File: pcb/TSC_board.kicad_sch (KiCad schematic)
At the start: 29 parts

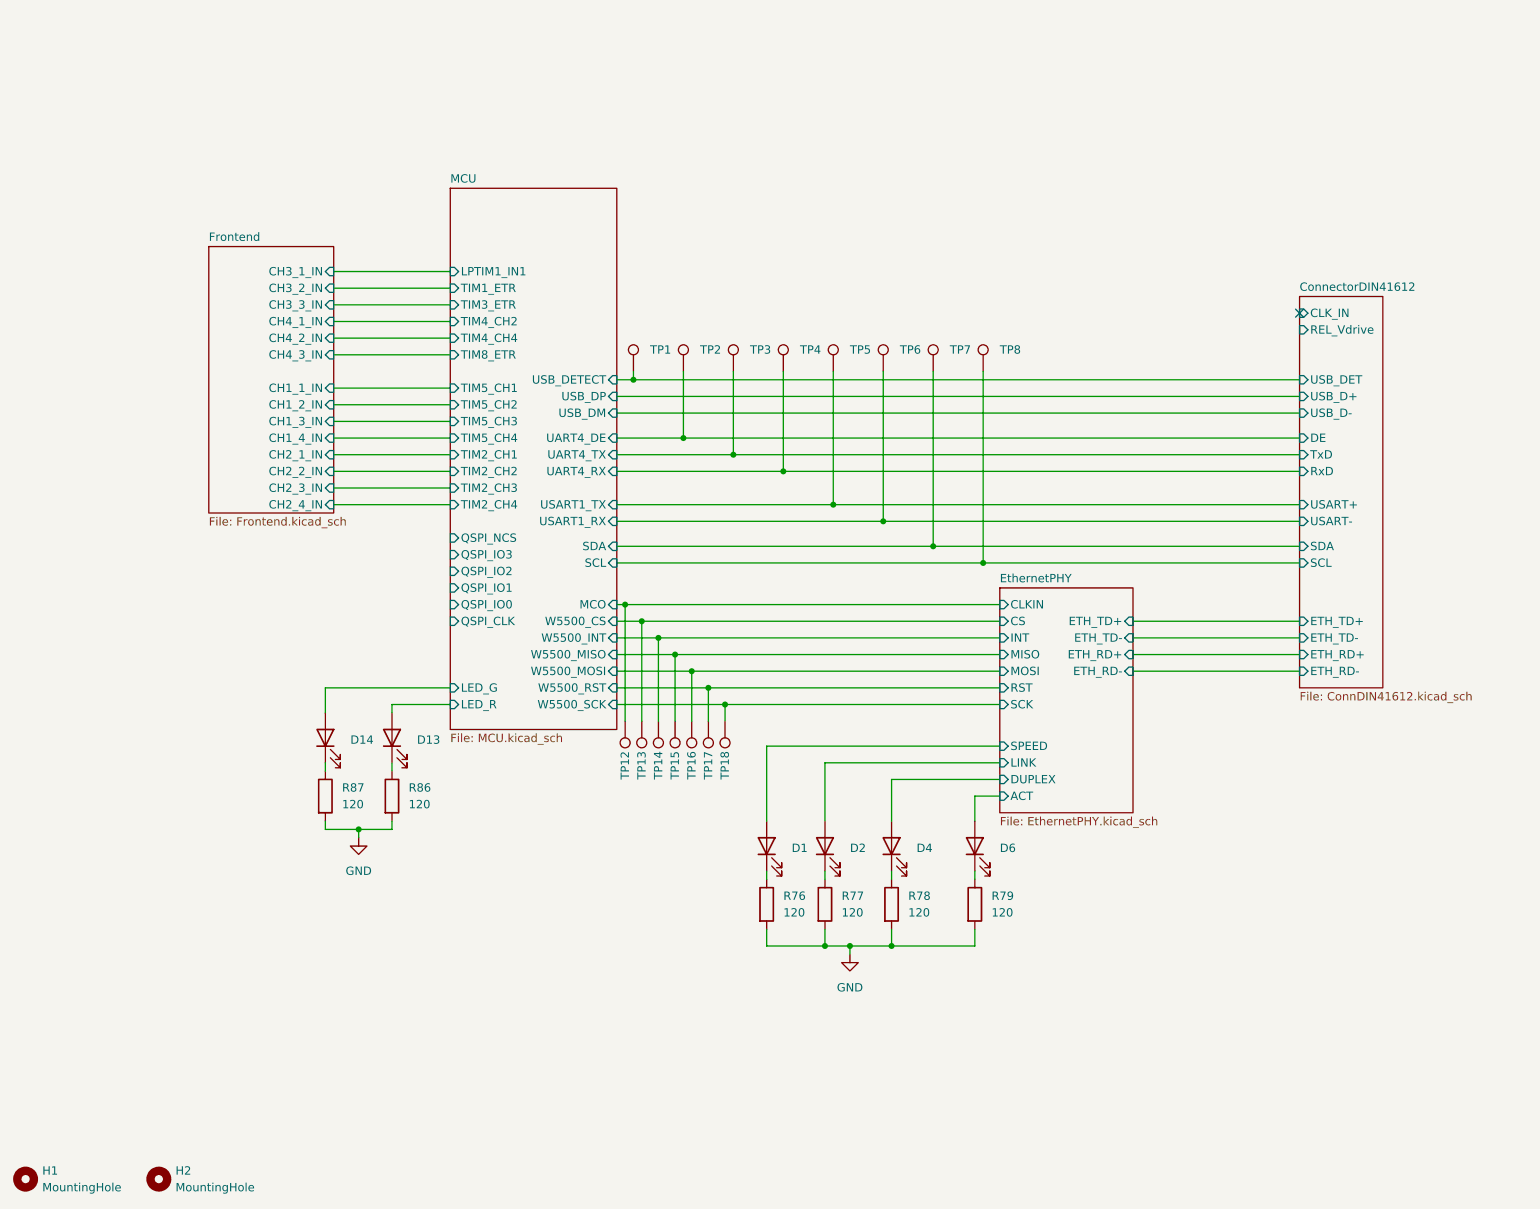
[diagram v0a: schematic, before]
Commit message: Change of concept, only frontend. To be connected with UCB_board
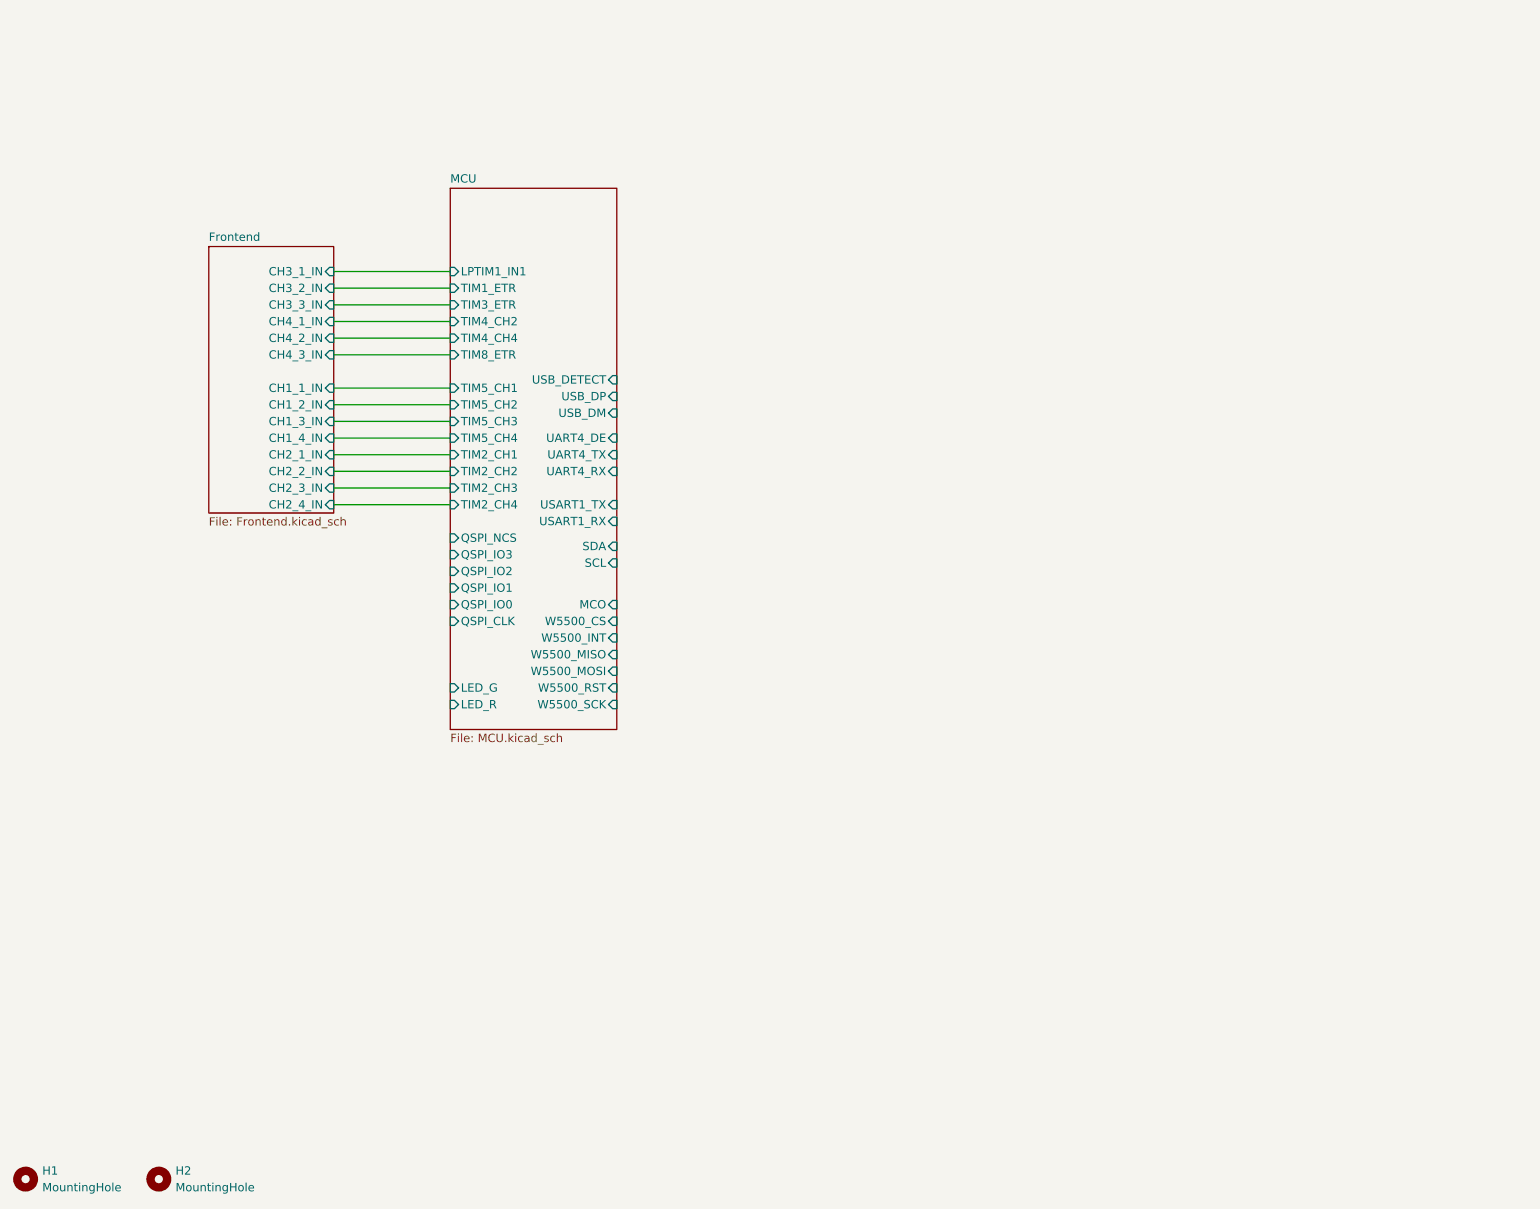
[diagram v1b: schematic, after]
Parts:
- removed D1, D13, D14, D2, D4, D6: ~, LED_SMD:LED_0603_1608Metric_Pad1.05x0.95mm_HandSolder, symbol Device:LED
- removed R76, R77, R78, R79, R86, R87: 120, Resistor_SMD:R_0603_1608Metric_Pad0.98x0.95mm_HandSolder, symbol Device:R
- removed TP1, TP12, TP13, TP14, TP15, TP16, TP17, TP18, TP2, TP3, TP4, TP5, TP6, TP7, TP8: TestPoint, TestPoint:TestPoint_Pad_D1.0mm, symbol Connector:TestPoint
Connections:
- no-connect marks 1 -> 0
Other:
- removed sheet ConnectorDIN41612
- removed sheet EthernetPHY

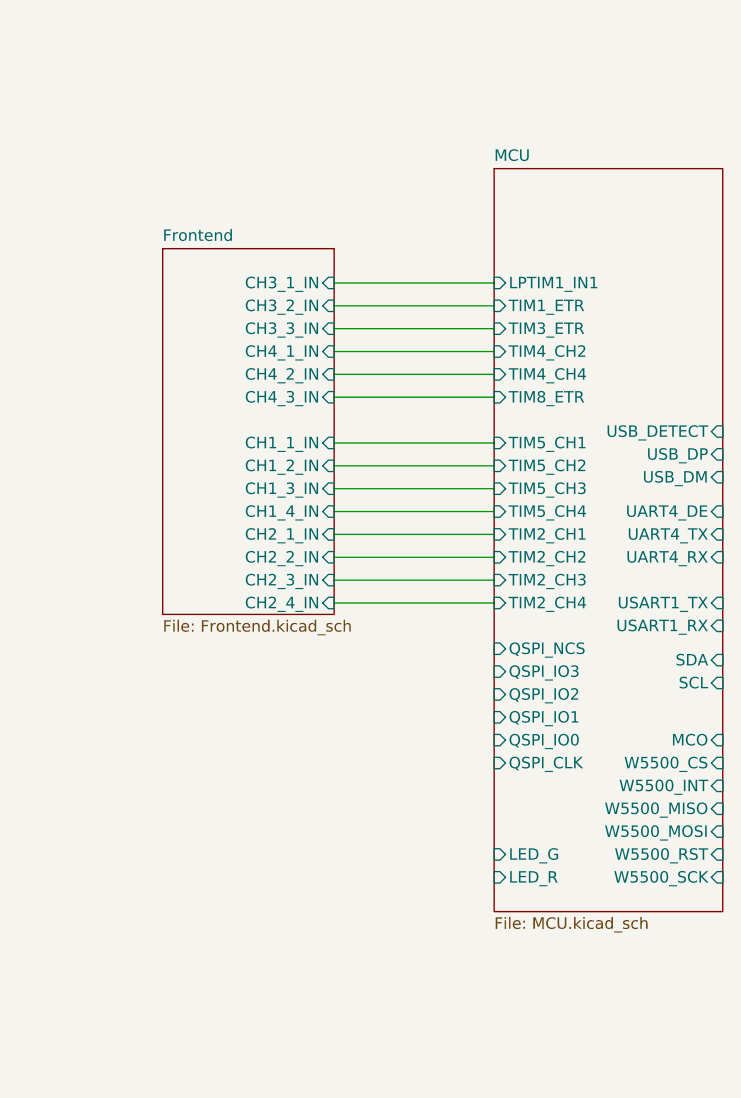
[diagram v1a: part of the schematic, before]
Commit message: Add STM32 .ioc and adjust UCB connector footprint
Add STM32CubeMX project file (firmware/TSC_board.ioc) for the STM32H563VITx MCU and update KiCad PCB/schematic files. Adjust UCB_conn footprint and apply corresponding changes to pcb TSC_board/Frontend/MCU schematic and project files to reflect the connector/placement updates.
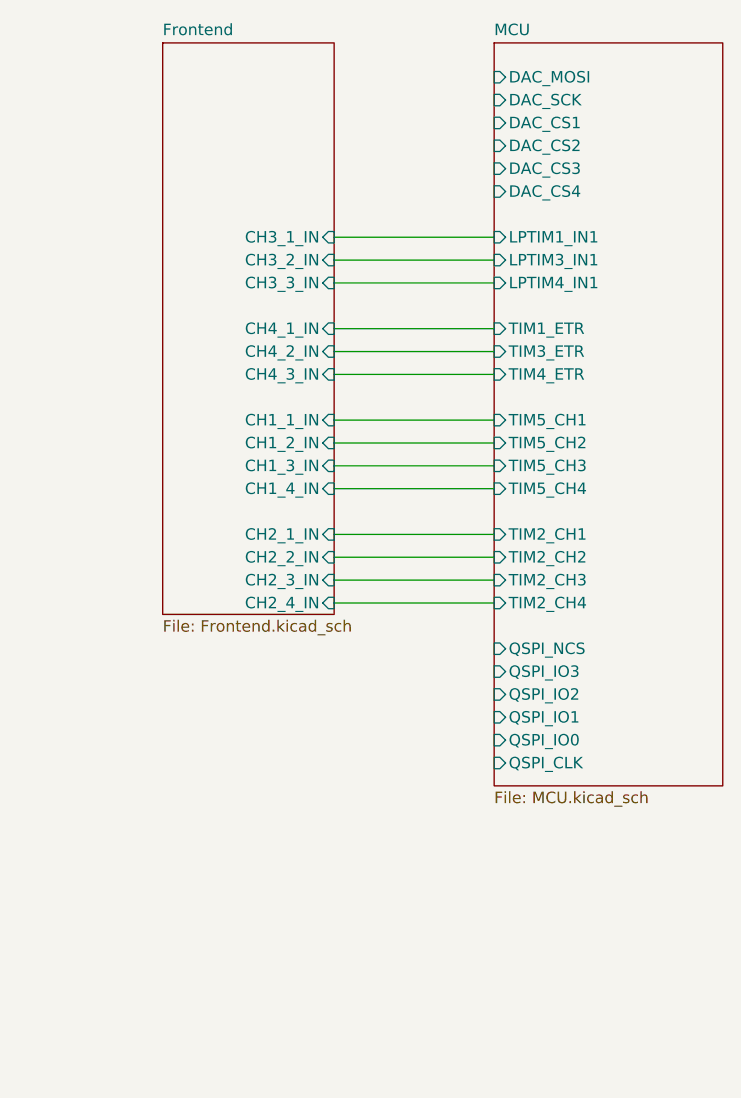
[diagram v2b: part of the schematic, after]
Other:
- sheet MCU ports: added DAC_CS1, DAC_CS2, DAC_CS3, DAC_CS4, DAC_MOSI, DAC_SCK, LPTIM3_IN1, LPTIM4_IN1, TIM4_ETR; removed LED_G, LED_R, MCO, SCL, SDA, TIM4_CH2, TIM4_CH4, TIM8_ETR, UART4_DE, UART4_RX, UART4_TX, USART1_RX, USART1_TX, USB_DETECT, USB_DM, USB_DP, W5500_CS, W5500_INT, W5500_MISO, W5500_MOSI, W5500_RST, W5500_SCK

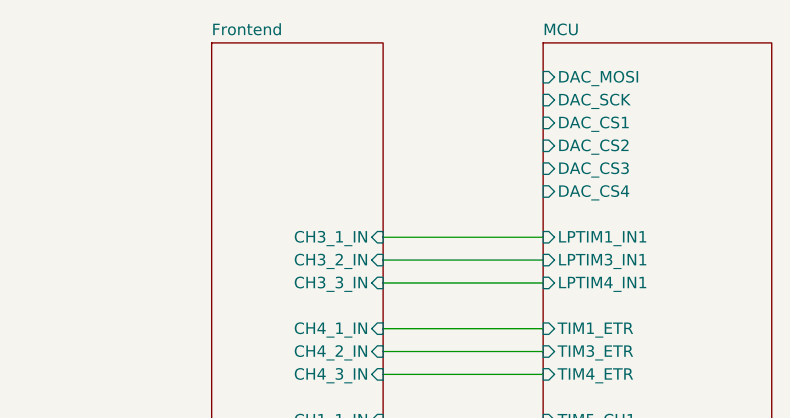
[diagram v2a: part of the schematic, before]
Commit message: Remove NL17SZ17 symbol; update schematic
Delete the NL17SZ17DFT2G symbol from pcb/Frontend.kicad_sch and apply a bulk update to schematic. Many junction coordinates and UUIDs were regenerated/adjusted in Frontend.kicad_sch; related KiCad files (pcb/MCU.kicad_sch, pcb/TSC_board.kicad_pcb, pcb/TSC_board.kicad_sch) were also updated. This is primarily a cleanup refresh.
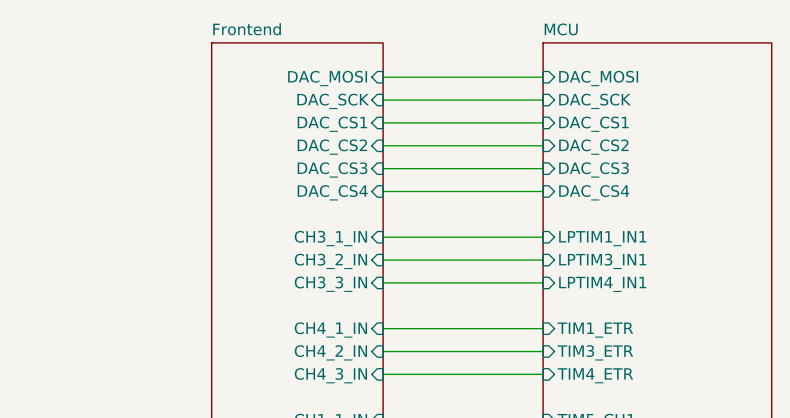
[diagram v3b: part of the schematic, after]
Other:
- sheet Frontend ports: added DAC_CS1, DAC_CS2, DAC_CS3, DAC_CS4, DAC_MOSI, DAC_SCK; removed none
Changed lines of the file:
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@@
+	(wire
+		(pts
+			(xy 68.58 31.75) (xy 86.36 31.75)
+		)
+		(stroke
+			(width 0)
+			(type default)
+		)
+	)
+	(wire
+		(pts
+			(xy 68.58 39.37) (xy 86.36 39.37)
+		)
+		(stroke
+			(width 0)
+			(type default)
+		)
+	)
+	(wire
+		(pts
+			(xy 68.58 36.83) (xy 86.36 36.83)
+		)
+		(stroke
+			(width 0)
+			(type default)
+		)
+	)
 	(wire
 		(pts
@@
 	(wire
 		(pts
+			(xy 68.58 34.29) (xy 86.36 34.29)
+		)
+		(stroke
+			(width 0)
+			(type default)
+		)
+	)
+	(wire
+		(pts
 			(xy 68.58 62.23) (xy 86.36 62.23)
 		)
@@
 	(wire
 		(pts
+			(xy 68.58 29.21) (xy 86.36 29.21)
+		)
+		(stroke
+			(width 0)
+			(type default)
+		)
+	)
+	(wire
+		(pts
 			(xy 68.58 82.55) (xy 86.36 82.55)
 		)
@@
 		(pts
 			(xy 68.58 85.09) (xy 86.36 85.09)
+		)
+		(stroke
+			(width 0)
+			(type default)
+		)
+	)
+	(wire
+		(pts
+			(xy 68.58 41.91) (xy 86.36 41.91)
 		)
 		(stroke
@@
 			(effects
 				(font
+					(size 1.27 1.27)
+				)
+				(justify right)
+			)
+		)
+		(pin "DAC_CS1" input
+			(at 68.58 34.29 0)
+			(effects
+				(font
+					(size 1.27 1.27)
+				)
+				(justify right)
+			)
+		)
+		(pin "DAC_CS2" input
+			(at 68.58 36.83 0)
+			(effects
+				(font
+					(size 1.27 1.27)
+				)
+				(justify right)
+			)
+		)
+		(pin "DAC_CS3" input
+			(at 68.58 39.37 0)
+			(effects
+				(font
+					(size 1.27 1.27)
+				)
+				(justify right)
+			)
+		)
+		(pin "DAC_MOSI" input
+			(at 68.58 29.21 0)
+			(effects
+				(font
+					(size 1.27 1.27)
+				)
+				(justify right)
+			)
+		)
+		(pin "DAC_SCK" input
+			(at 68.58 31.75 0)
+			(effects
+				(font
+					(size 1.27 1.27)
+				)
+				(justify right)
+			)
+		)
+		(pin "DAC_CS4" input
+			(at 68.58 41.91 0)
+			(effects
+				(font

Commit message: Update TSC_board schematic and layout
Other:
- sheet MCU renamed Conn
- added sheet RAM (RAM.kicad_sch)
- sheet Conn: file MCU.kicad_sch -> Conn.kicad_sch

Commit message: Before DRC
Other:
- sheet Conn ports: added UART_RX, UART_TX; removed none
- sheet Frontend ports: added UART_RX, UART_TX; removed none
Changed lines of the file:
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@@
+	(wire
+		(pts
+			(xy 161.29 31.75) (xy 179.07 31.75)
+		)
+		(stroke
+			(width 0)
+			(type default)
+		)
+	)
 	(wire
 		(pts
@@
 		(pts
 			(xy 161.29 96.52) (xy 179.07 96.52)
+		)
+		(stroke
+			(width 0)
+			(type default)
+		)
+	)
+	(wire
+		(pts
+			(xy 161.29 34.29) (xy 179.07 34.29)
 		)
 		(stroke
@@
 	)
 	(sheet
-		(at 142.24 36.83)
-		(size 19.05 63.5)
+		(at 142.24 27.94)
+		(size 19.05 72.39)
 		(exclude_from_sim no)
 		(in_bom yes)
@@
 		)
 		(property "Sheetname" "Frontend"
-			(at 142.24 36.1184 0)
+			(at 142.24 27.2284 0)
 			(effects
 				(font
@@
 		(pin "DAC_CS4" input
 			(at 161.29 53.34 0)
+			(effects
+				(font
+					(size 1.27 1.27)
+				)
+				(justify right)
+			)
+		)
+		(pin "UART_RX" input
+			(at 161.29 31.75 0)
+			(effects
+				(font
+					(size 1.27 1.27)
+				)
+				(justify right)
+			)
+		)
+		(pin "UART_TX" input
+			(at 161.29 34.29 0)
 			(effects
 				(font
@@
 	)
 	(sheet
-		(at 179.07 36.83)
-		(size 25.4 87.63)
+		(at 179.07 27.94)
+		(size 25.4 96.52)
 		(exclude_from_sim no)
 		(in_bom yes)
@@
 		)
 		(property "Sheetname" "Conn"
-			(at 179.07 36.1184 0)
+			(at 179.07 27.2284 0)
 			(effects
 				(font
@@
 			(effects
 				(font
+					(size 1.27 1.27)
+				)
+				(justify left)
+			)
+		)
+		(pin "UART_RX" input
+			(at 179.07 31.75 180)
+			(effects
+				(font
+					(size 1.27 1.27)
+				)
+				(justify left)
+			)
+		)
+		(pin "UART_TX" input
+			(at 179.07 34.29 180)
+			(effects
+				(font

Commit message: Finished r0
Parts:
- added R205: 10k, Resistor_SMD:R_0603_1608Metric, symbol Device:R
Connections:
- net Conn/UART_TX: now also R205.2
- new net +3.3V: R205.1
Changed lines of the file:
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@@
 		(rev "0.1")
 	)
+	(junction
+		(at 168.91 34.29)
+		(diameter 0)
+		(color 0 0 0 0)
+	)
 	(wire
 		(pts
@@
 	(wire
 		(pts
+			(xy 168.91 19.05) (xy 168.91 21.59)
+		)
+		(stroke
+			(width 0)
+			(type default)
+		)
+	)
+	(wire
+		(pts
 			(xy 161.29 50.8) (xy 179.07 50.8)
 		)
@@
 	(wire
 		(pts
+			(xy 168.91 34.29) (xy 179.07 34.29)
+		)
+		(stroke
+			(width 0)
+			(type default)
+		)
+	)
+	(wire
+		(pts
 			(xy 161.29 68.58) (xy 179.07 68.58)
 		)
@@
 	(wire
 		(pts
+			(xy 168.91 29.21) (xy 168.91 34.29)
+		)
+		(stroke
+			(width 0)
+			(type default)
+		)
+	)
+	(wire
+		(pts
 			(xy 161.29 31.75) (xy 179.07 31.75)
 		)
@@
 	(wire
 		(pts
-			(xy 161.29 34.29) (xy 179.07 34.29)
+			(xy 161.29 34.29) (xy 168.91 34.29)
 		)
 		(stroke
@@
 			(width 0)
 			(type default)
+		)
+	)
+	(symbol
+		(lib_id "power:+3.3V")
+		(at 168.91 19.05 0)
+		(unit 1)
+		(exclude_from_sim no)
+		(in_bom yes)
+		(on_board yes)
+		(dnp no)
+		(fields_autoplaced yes)
+		(property "Reference" "#PWR063"
+			(at 168.91 22.86 0)
+			(effects
+				(font
+					(size 1.27 1.27)
+				)
+				(hide yes)
+			)
+		)
+		(property "Value" "+3.3V"
+			(at 168.91 13.97 0)
+			(effects
+				(font
+					(size 1.27 1.27)
+				)
+			)
+		)
+		(property "Footprint" ""
+			(at 168.91 19.05 0)
+			(effects
+				(font
+					(size 1.27 1.27)
+				)
+				(hide yes)
+			)
+		)
+		(property "Datasheet" ""
+			(at 168.91 19.05 0)
+			(effects
+				(font
+					(size 1.27 1.27)
+				)
+				(hide yes)
+			)
+		)
+		(property "Description" "Power symbol creates a global label with name \"+3.3V\""
+			(at 168.91 19.05 0)
+			(effects
+				(font
+					(size 1.27 1.27)
+				)
+				(hide yes)
+			)
+		)
+		(pin "1"
+		)
+		(instances
+			(project "TSC_board"
+				(path "/0c4edb77-9bdf-4103-be66-c5eb9940b163"
+					(reference "#PWR063")
+					(unit 1)
+				)
+			)
 		)
 	)
@@
 					(unit 1)
 				)
+			)
+		)
+	)
+	(symbol
+		(lib_id "Device:R")
+		(at 168.91 25.4 0)
+		(unit 1)
+		(exclude_from_sim no)
+		(in_bom yes)
+		(on_board yes)
+		(dnp no)
+		(fields_autoplaced yes)
+		(property "Reference" "R205"
+			(at 171.45 24.1299 0)
+			(effects
+				(font
+					(size 1.27 1.27)
+				)
+				(justify left)
+			)
+		)
+		(property "Value" "10k"
+			(at 171.45 26.6699 0)
+			(effects
+				(font
+					(size 1.27 1.27)
+				)
+				(justify left)
+			)
+		)
+		(property "Footprint" "Resistor_SMD:R_0603_1608Metric"
+			(at 167.132 25.4 90)
+			(effects
+				(font
+					(size 1.27 1.27)
+				)
+				(hide yes)
+			)
+		)
+		(property "Datasheet" "~"
+			(at 168.91 25.4 0)
+			(effects
+				(font
+					(size 1.27 1.27)
+				)
+				(hide yes)
+			)
+		)
+		(property "Description" "Resistor"
+			(at 168.91 25.4 0)
+			(effects
+				(font
+					(size 1.27 1.27)
+				)
+				(hide yes)
+			)
+		)
+		(pin "2"
+		)
+		(pin "1"
+		)
+		(instances
+			(project "TSC_board"
+				(path "/0c4edb77-9bdf-4103-be66-c5eb9940b163"
+					(reference "R205")
+					(unit 1)
+				)
